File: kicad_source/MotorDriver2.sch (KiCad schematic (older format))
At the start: 25 parts, among them P3 CONN_01X04, P4 CONN_01X05, U1 TMC5130A-TA

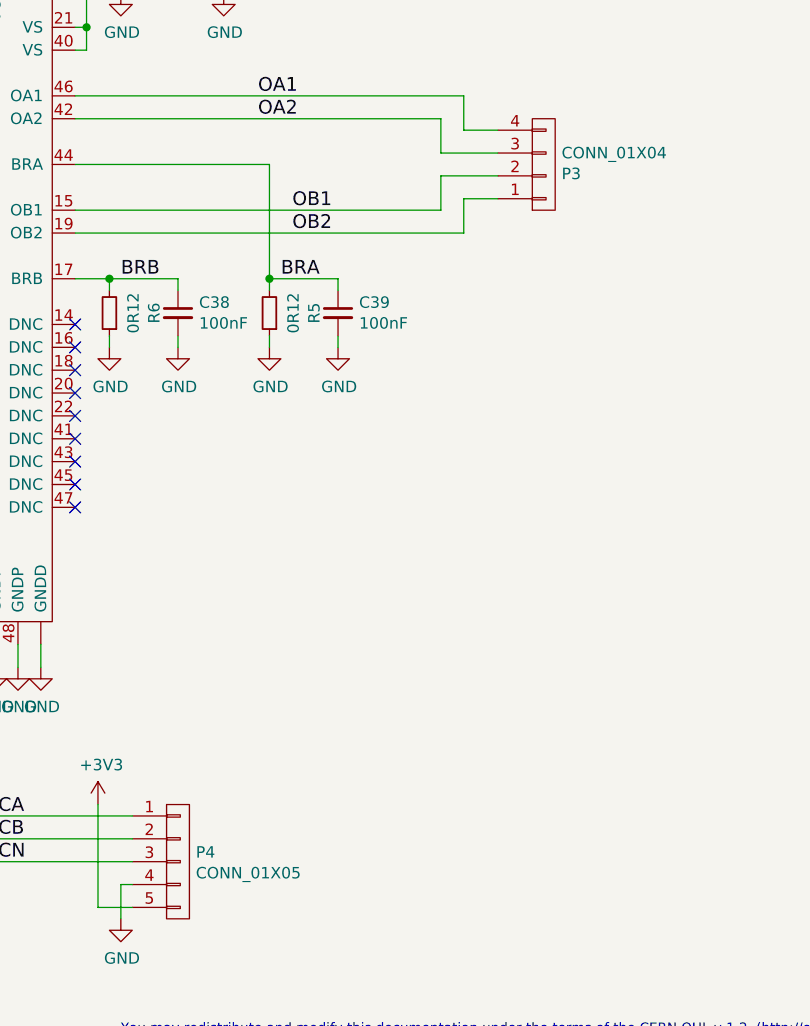
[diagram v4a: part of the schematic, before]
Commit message: changed type of encoder connector
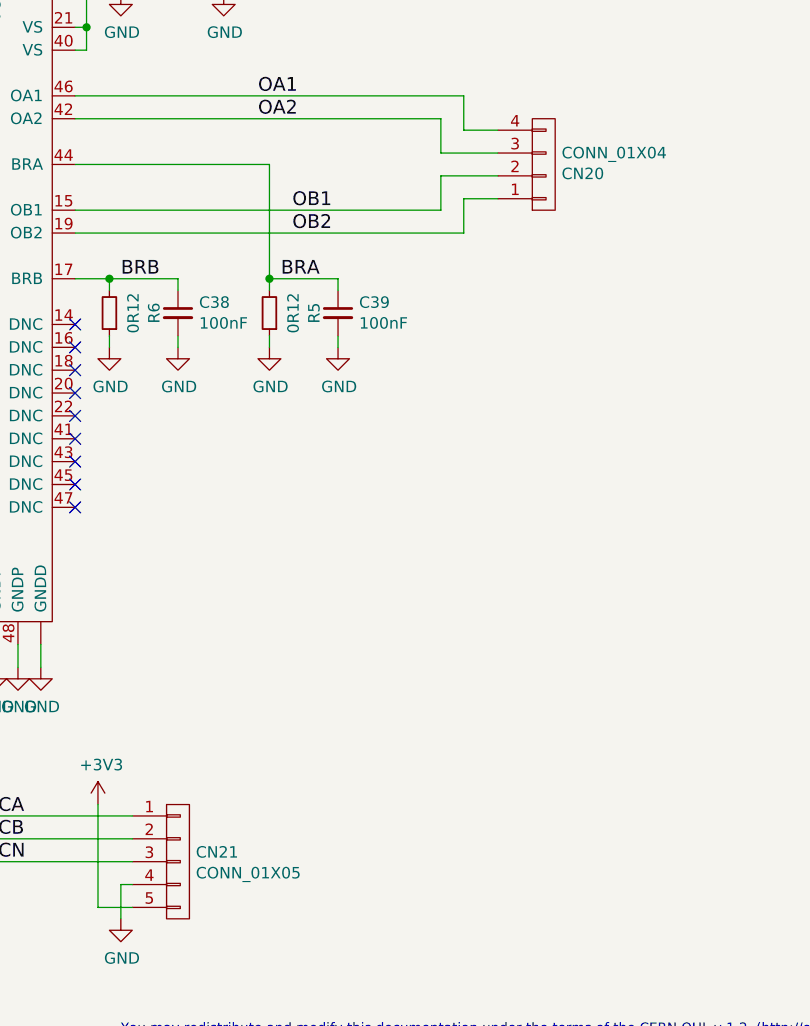
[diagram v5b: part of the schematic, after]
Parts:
- CN21: renamed from P4; footprint CON_wuerth:WR-TBL_691322310005 -> connectors_JST_PH:Connectors_JST_S5B-PH-SM4-TB
- renumbered P3 to CN20
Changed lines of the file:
@@
 NoConn ~ 5300 5050
 $Comp
-L mechanical-connectors:CONN_01X05 P4
+L mechanical-connectors:CONN_01X05 CN21
 U 1 1 5DF646C3
 P 7250 6000
-F 0 "P4" H 7328 6041 50  0000 L CNN
+F 0 "CN21" H 7328 6041 50  0000 L CNN
 F 1 "CONN_01X05" H 7328 5950 50  0000 L CNN
-F 2 "CON_wuerth:WR-TBL_691322310005" H 7250 6000 50  0001 C CNN
+F 2 "connectors_JST_PH:Connectors_JST_S5B-PH-SM4-TB" H 7250 6000 50  0001 C CNN
 F 3 "" H 7250 6000 50  0000 C CNN
 	1    7250 6000
@@
 	4750 5700 5950 5700
 $Comp
-L mechanical-connectors:CONN_01X04 P3
+L mechanical-connectors:CONN_01X04 CN20
 U 1 1 5DED18D8
 P 8850 2950
-F 0 "P3" H 8928 2991 50  0000 L CNN
+F 0 "CN20" H 8928 2991 50  0000 L CNN
 F 1 "CONN_01X04" H 8928 2900 50  0000 L CNN
 F 2 "CON_wuerth:WR-TBL_691322310004" H 8850 2950 50  0001 C CNN

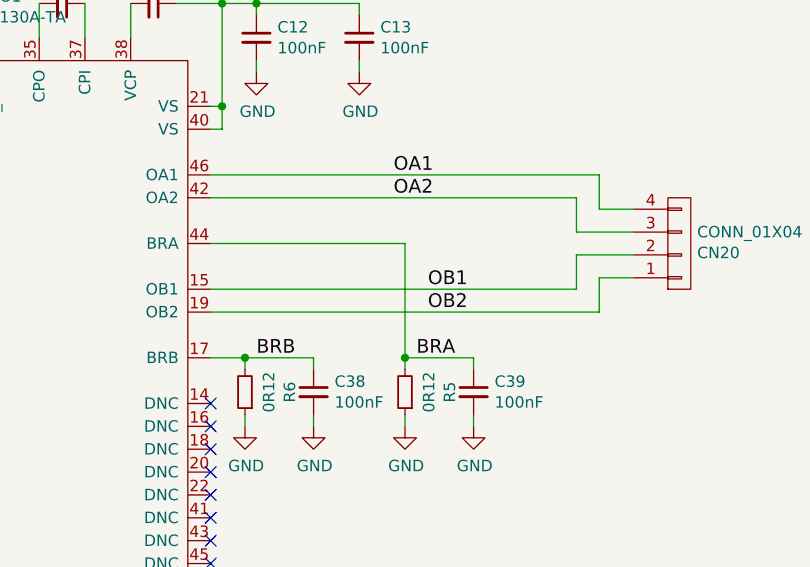
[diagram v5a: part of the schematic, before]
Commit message: updated layout
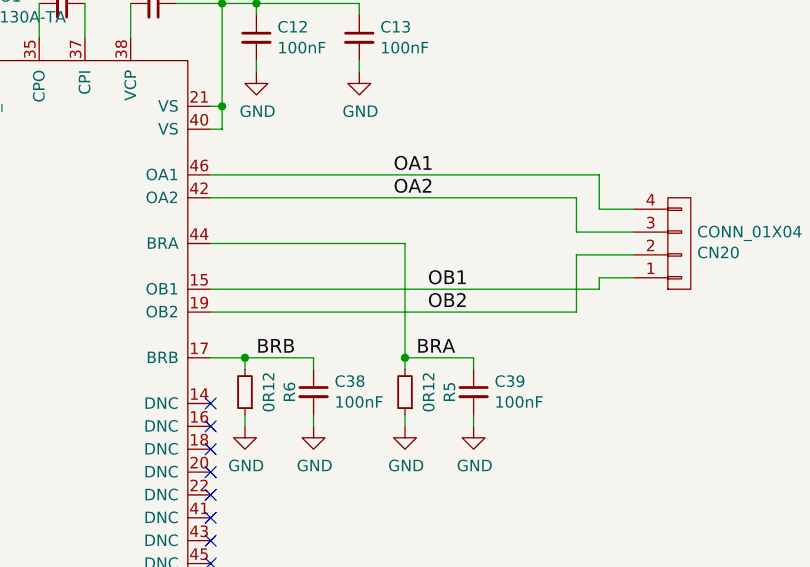
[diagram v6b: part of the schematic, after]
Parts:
- CN21: footprint connectors_JST_PH:Connectors_JST_S5B-PH-SM4-TB -> connectors_JST_SH:Connectors_JST_BM05B-SRSS-TB
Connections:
- net OB1: now also CN20.1 (P1); no longer CN20.2 (P2)
- net OB2: now also CN20.2 (P2); no longer CN20.1 (P1)
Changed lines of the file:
@@
 $EndComp
-Wire Wire Line
-	6800 3150 8400 3150
-Wire Wire Line
-	8400 3150 8400 3000
 Wire Wire Line
 	8400 3000 8650 3000
 Wire Wire Line
-	6800 3250 8500 3250
-Wire Wire Line
-	8500 3250 8500 3100
+	6800 3250 8400 3250
 Wire Wire Line
 	8500 3100 8650 3100
@@
 F 0 "CN21" H 7328 6041 50  0000 L CNN
 F 1 "CONN_01X05" H 7328 5950 50  0000 L CNN
-F 2 "connectors_JST_PH:Connectors_JST_S5B-PH-SM4-TB" H 7250 6000 50  0001 C CNN
+F 2 "connectors_JST_SH:Connectors_JST_BM05B-SRSS-TB" H 7250 6000 50  0001 C CNN
 F 3 "" H 7250 6000 50  0000 C CNN
 	1    7250 6000
@@
 Wire Wire Line
 	6800 2950 7650 2950
+Wire Wire Line
+	8500 3150 8500 3100
+Wire Wire Line
+	6800 3150 8500 3150
+Wire Wire Line
+	8400 3000 8400 3250
 $EndSCHEMATC

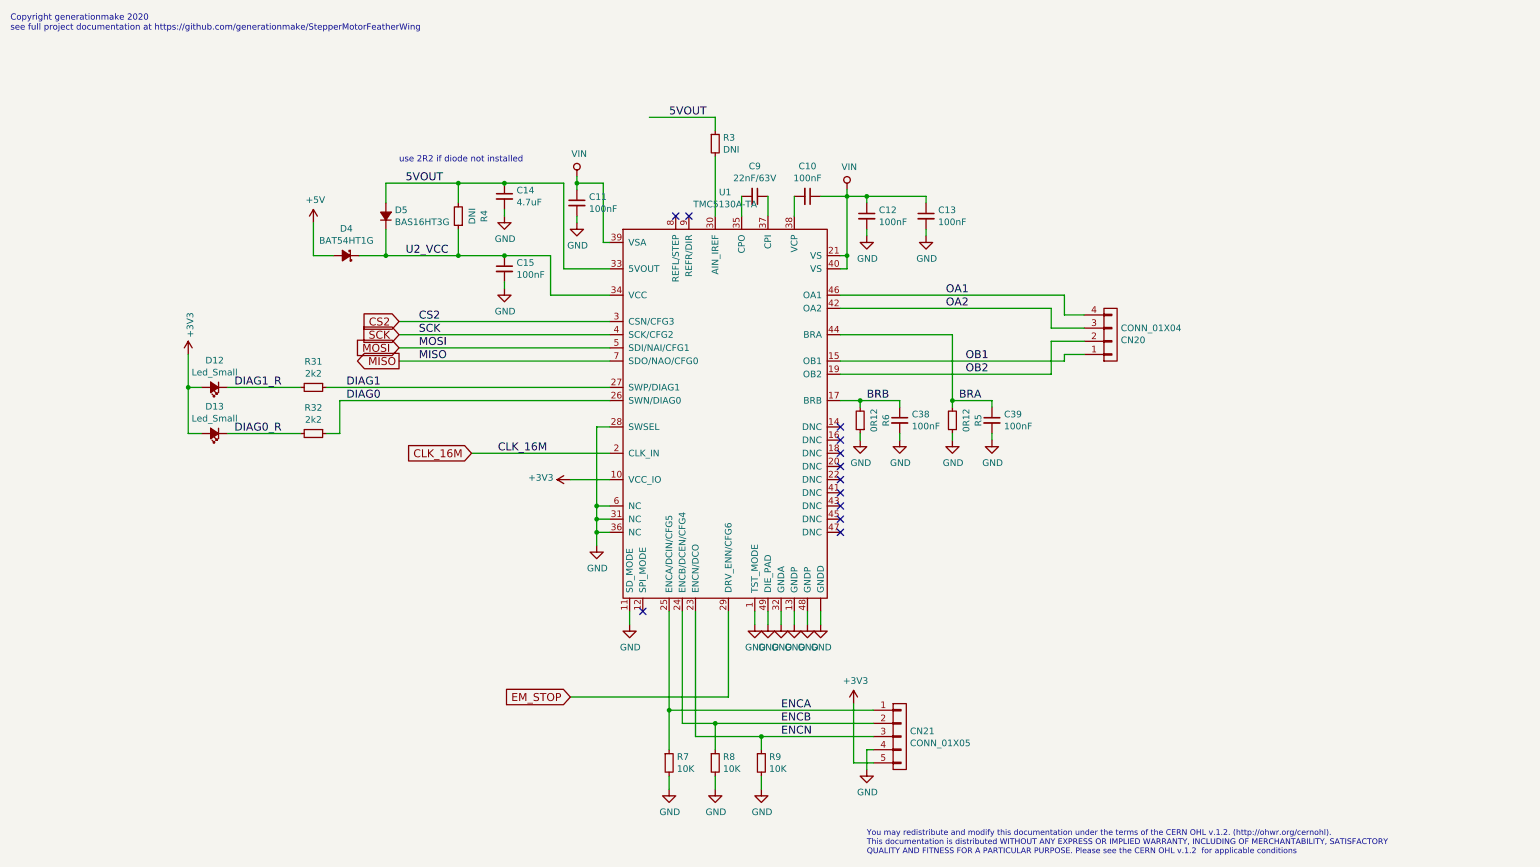
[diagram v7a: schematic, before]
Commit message: updated part numbers
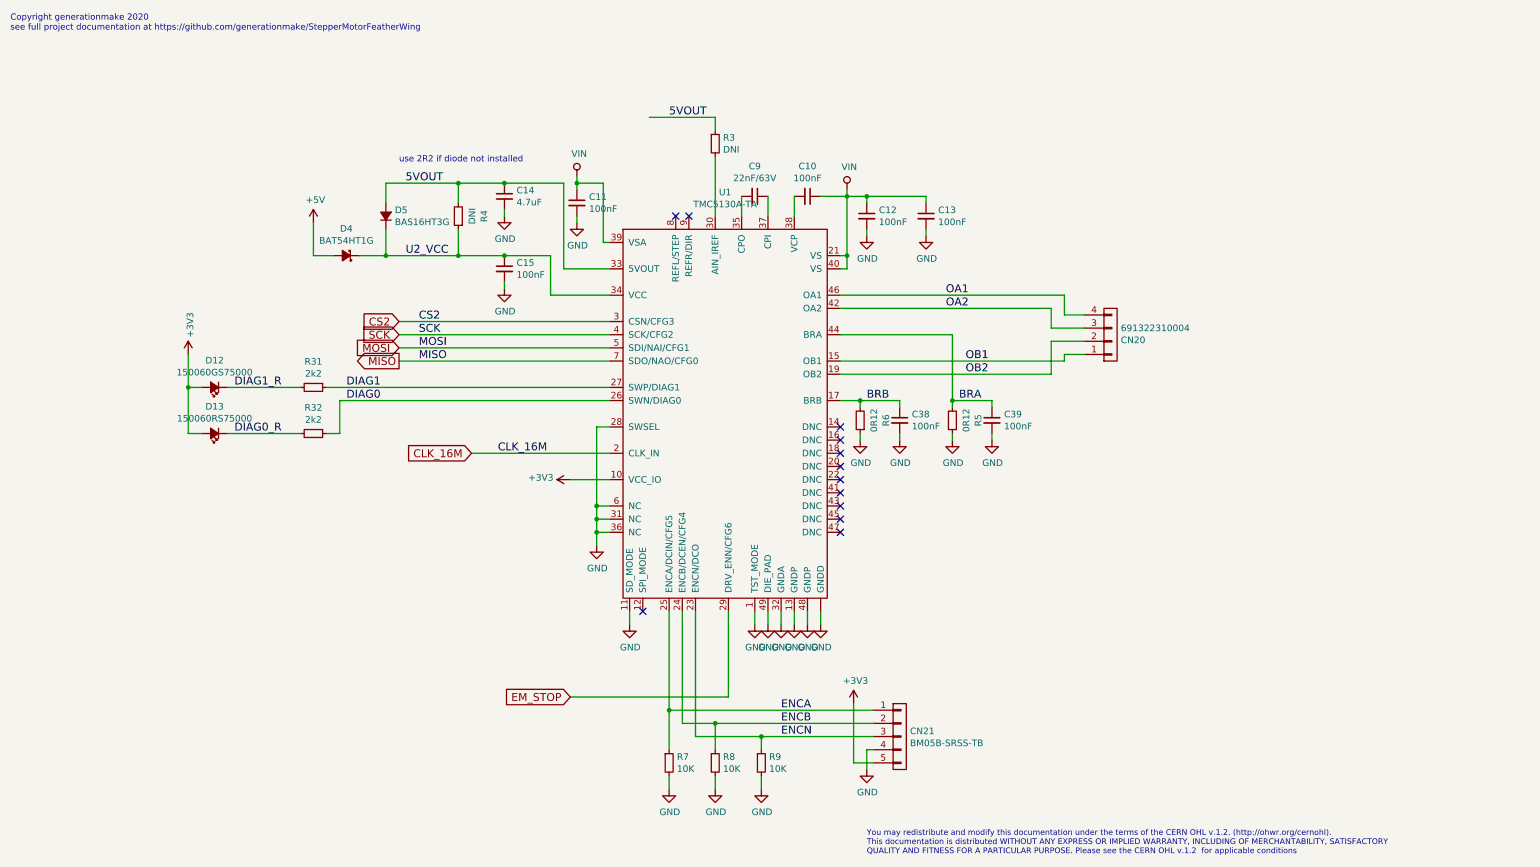
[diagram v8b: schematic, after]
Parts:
- CN20: value CONN_01X04 -> 691322310004
- CN21: value CONN_01X05 -> BM05B-SRSS-TB
- D12: value Led_Small -> 150060GS75000
- D13: value Led_Small -> 150060RS75000
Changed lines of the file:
@@
 P 7250 6000
 F 0 "CN21" H 7328 6041 50  0000 L CNN
-F 1 "CONN_01X05" H 7328 5950 50  0000 L CNN
+F 1 "BM05B-SRSS-TB" H 7328 5950 50  0000 L CNN
 F 2 "connectors_JST_SH:Connectors_JST_BM05B-SRSS-TB" H 7250 6000 50  0001 C CNN
 F 3 "" H 7250 6000 50  0000 C CNN
@@
 P 8850 2950
 F 0 "CN20" H 8928 2991 50  0000 L CNN
-F 1 "CONN_01X04" H 8928 2900 50  0000 L CNN
+F 1 "691322310004" H 8928 2900 50  0000 L CNN
 F 2 "CON_wuerth:WR-TBL_691322310004" H 8850 2950 50  0001 C CNN
 F 3 "" H 8850 2950 50  0000 C CNN
@@
 AR Path="/5DE3616E/5F0A0DDE" Ref="D12"  Part="1"
 F 0 "D12" H 2050 3145 50  0000 C CNN
-F 1 "Led_Small" H 2050 3236 50  0000 C CNN
+F 1 "150060GS75000" H 2050 3236 50  0000 C CNN
 F 2 "LEDs:LED_0603" V 2050 3350 50  0001 C CNN
 F 3 "" V 2050 3350 50  0000 C CNN
@@
 AR Path="/5DE3616E/5F0A0DEA" Ref="D13"  Part="1"
 F 0 "D13" H 2050 3495 50  0000 C CNN
-F 1 "Led_Small" H 2050 3586 50  0000 C CNN
+F 1 "150060RS75000" H 2050 3586 50  0000 C CNN
 F 2 "LEDs:LED_0603" V 2050 3700 50  0001 C CNN
 F 3 "" V 2050 3700 50  0000 C CNN
